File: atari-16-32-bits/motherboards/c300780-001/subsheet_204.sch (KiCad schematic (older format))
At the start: 16 parts, among them J204 RS-232 Serial Port, U206 MC1488_QUAD_LINE_EIA-232D_DRI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, U207 MC1489_QUAD_LINE_EIA-232D_REC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

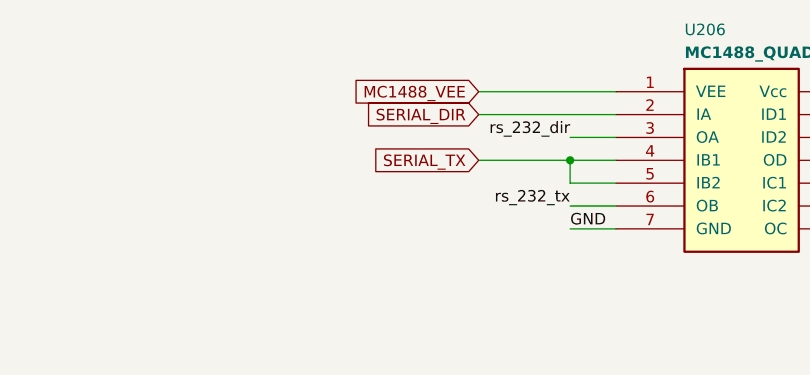
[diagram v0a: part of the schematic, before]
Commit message: rename global label feeding mc1488 vee into '-12V'
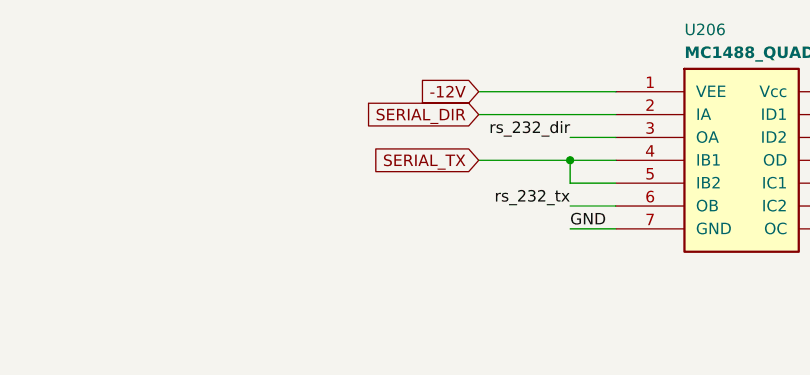
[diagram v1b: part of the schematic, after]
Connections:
- net MC1488_VEE renamed -12V
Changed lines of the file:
@@
 GND
 Text GLabel 3100 1800 0    50   Input ~ 0
-MC1488_VEE
+-12V
 Text GLabel 3100 2100 0    50   Input ~ 0
 SERIAL_TX

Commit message: done sheet 2
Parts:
- added C206: 0.1uF, symbol Device:C
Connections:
- net G12V: now also C206.1
- net GND: now also C206.2
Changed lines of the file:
@@
 $Descr A4 8268 11693 portrait
 encoding utf-8
-Sheet 13 13
+Sheet 13 14
 Title ""
 Date ""
@@
 	1    0    0    -1
 $EndComp
+$Comp
+L Device:C C206
+U 1 1 609CC7B6
+P 6500 2050
+F 0 "C206" H 6525 2150 50  0000 L CNN
+F 1 "0.1uF" H 6525 1950 50  0000 L CNN
+F 2 "" H 6538 1900 50  0001 C CNN
+F 3 "~" H 6500 2050 50  0001 C CNN
+	1    6500 2050
+	1    0    0    -1
+$EndComp
+Text Label 6500 2400 1    50   ~ 0
+GND
+Wire Wire Line
+	6500 2200 6500 2400
+Wire Wire Line
+	6500 1700 6500 1900
+Text GLabel 6500 1700 1    50   Input ~ 0
+G12V
 $EndSCHEMATC
